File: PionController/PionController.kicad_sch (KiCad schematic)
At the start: 1 part, among them U1 STM32H743VITx

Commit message: power
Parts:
- U1: LCSC (none) -> C1235410; Manufacturer (none) -> stm32f413vgt3
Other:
- added sheet power (untitled.kicad_sch)
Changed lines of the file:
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@@
+			)
+		)
+		(property "LCSC" "C1235410"
+			(at 106.68 100.33 0)
+			(effects
+				(font
+					(size 1.27 1.27)
+				)
+				(hide yes)
+			)
+		)
+		(property "Manufacturer" "stm32f413vgt3"
+			(at 106.68 100.33 0)
+			(effects
+				(font
+					(size 1.27 1.27)
+				)
+				(hide yes)
 			)
 		)
@@
 				)
 			)
+		)
+	)
+	(sheet
+		(at 387.35 137.16)
+		(size 34.29 31.75)
+		(fields_autoplaced yes)
+		(stroke
+			(width 0.1524)
+			(type solid)
+		)
+		(fill
+			(color 0 0 0 0.0000)
+		)
+		(property "Sheetname" "power"
+			(at 387.35 136.4484 0)
+			(effects
+				(font
+					(size 1.27 1.27)
+				)
+				(justify left bottom)
+			)
+		)
+		(property "Sheetfile" "untitled.kicad_sch"
+			(at 387.35 169.4946 0)
+			(effects
+				(font
+					(size 1.27 1.27)
+				)
+				(justify left top)
+			)
+		)
+		(property "Field2" ""
+			(at 387.35 137.16 0)
+			(effects
+				(font
+					(size 1.27 1.27)
+				)
+				(hide yes)
+			)
+		)
+		(instances
+			(project "PionController"
+				(path "/4c75befe-3f28-4e3b-aaa6-2731a1e568ad"
+					(page "2")
+				)
+			)

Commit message: Power_Fix
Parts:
- removed U1: STM32H743VITx, Package_QFP:LQFP-100_14x14mm_P0.5mm, symbol MCU_ST_STM32H7:STM32H743VITx
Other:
- added sheet Main (main.kicad_sch)

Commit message: Schematic_ready
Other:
- added sheet CAN (CAN.kicad_sch)
- added sheet Connectors (connectors.kicad_sch)
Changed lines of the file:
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@@
 	(paper "A4")
+	(sheet
+		(at 198.12 17.78)
+		(size 39.37 30.48)
+		(fields_autoplaced yes)
+		(stroke
+			(width 0.1524)
+			(type solid)
+		)
+		(fill
+			(color 0 0 0 0.0000)
+		)
+		(property "Sheetname" "CAN"
+			(at 198.12 17.0684 0)
+			(effects
+				(font
+					(size 1.27 1.27)
+				)
+				(justify left bottom)
+			)
+		)
+		(property "Sheetfile" "CAN.kicad_sch"
+			(at 198.12 48.8446 0)
+			(effects
+				(font
+					(size 1.27 1.27)
+				)
+				(justify left top)
+			)
+		)
+		(instances
+			(project "PionController"
+				(path "/4c75befe-3f28-4e3b-aaa6-2731a1e568ad"
+					(page "4")
+				)
+			)
+		)
+	)
 	(sheet
 		(at 245.11 59.69)
@@
 				)
 			)
+		)
+	)
+	(sheet
+		(at 199.39 60.96)
+		(size 38.1 49.53)
+		(fields_autoplaced yes)
+		(stroke
+			(width 0.1524)
+			(type solid)
+		)
+		(fill
+			(color 0 0 0 0.0000)
+		)
+		(property "Sheetname" "Connectors"
+			(at 199.39 60.2484 0)
+			(effects
+				(font
+					(size 1.27 1.27)
+				)
+				(justify left bottom)
+			)
+		)
+		(property "Sheetfile" "connectors.kicad_sch"
+			(at 199.39 111.0746 0)
+			(effects
+				(font
+					(size 1.27 1.27)
+				)
+				(justify left top)
+			)
+		)
+		(instances
+			(project "PionController"
+				(path "/4c75befe-3f28-4e3b-aaa6-2731a1e568ad"
+					(page "5")
+				)
+			)

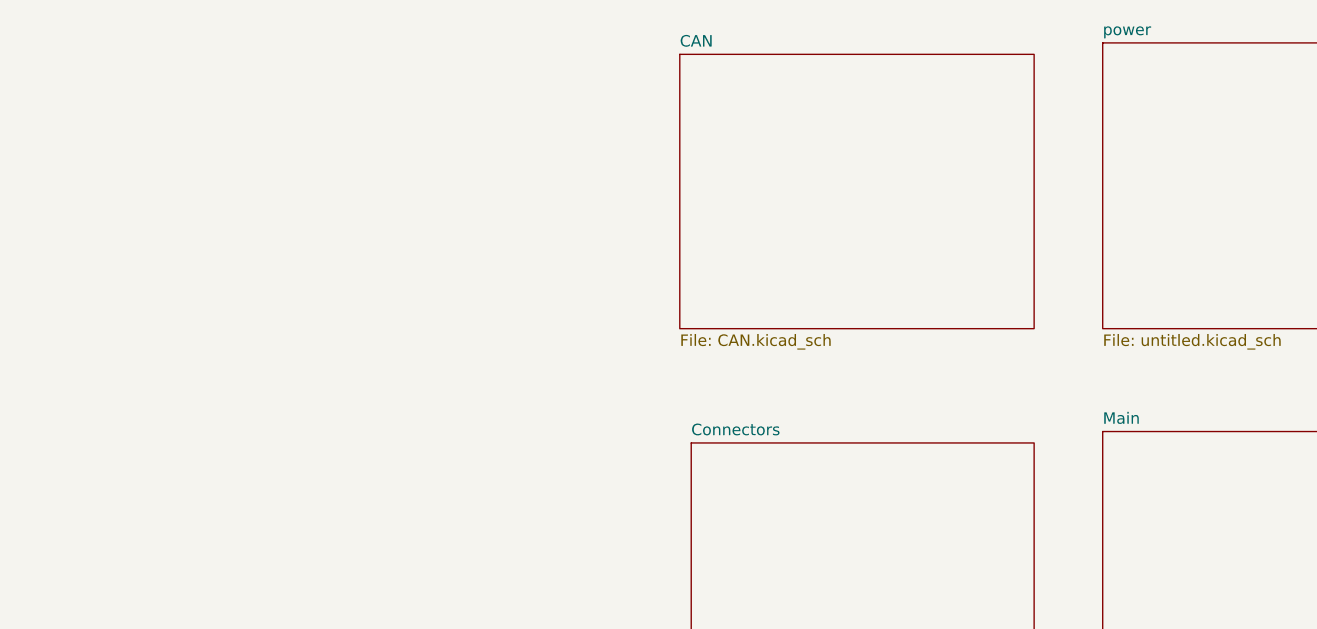
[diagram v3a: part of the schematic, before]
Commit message: adding board outline
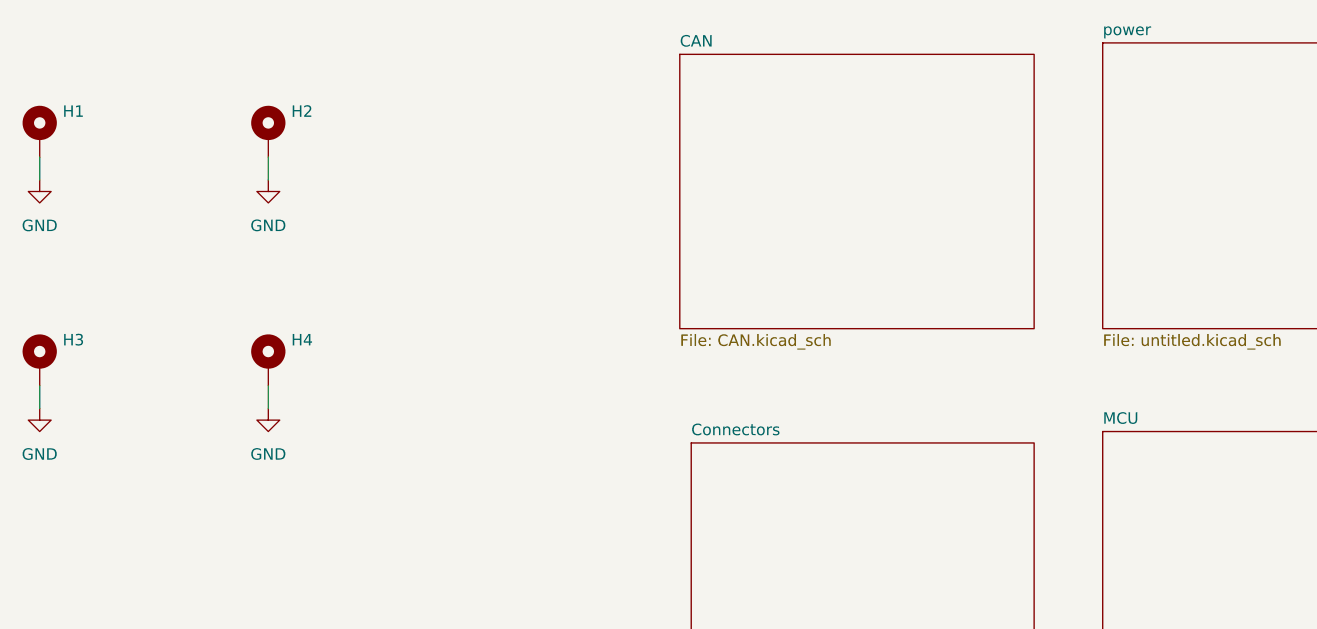
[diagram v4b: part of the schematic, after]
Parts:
- added H1, H2, H3, H4: MountingHole_Pad, MountingHole:MountingHole_3.2mm_M3_Pad_Via, symbol Mechanical:MountingHole_Pad
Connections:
- new net GND: H1.1, H2.1, H3.1, H4.1
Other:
- sheet Main renamed MCU

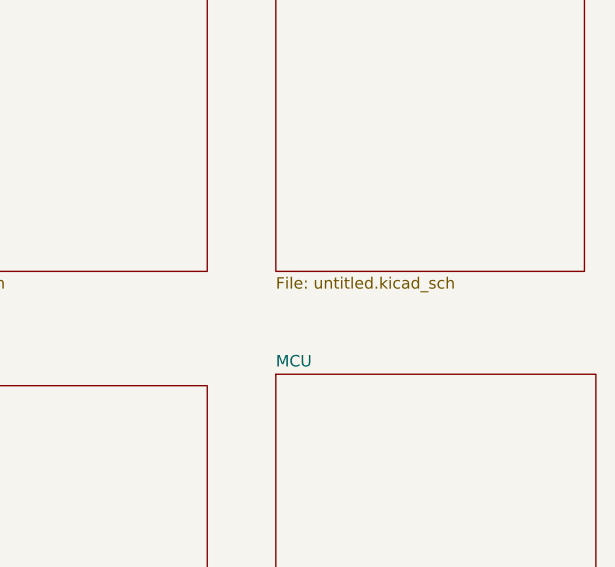
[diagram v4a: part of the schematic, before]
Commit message: Fixing Ivan's remarks and adding the forgotten pull-down resistor
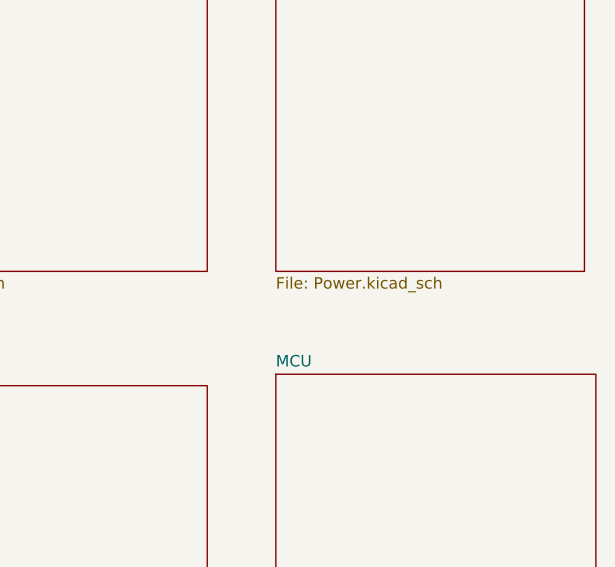
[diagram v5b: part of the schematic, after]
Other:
- sheet power: file untitled.kicad_sch -> Power.kicad_sch
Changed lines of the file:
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@@
 			)
 		)
-		(property "Sheetfile" "untitled.kicad_sch"
+		(property "Sheetfile" "Power.kicad_sch"
 			(at 245.11 48.8446 0)
 			(effects

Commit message: Fixed reference designators in SCH and moved PCB silkscreen positions for better visibility
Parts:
- H1, H2, H3, H4: LCSC (none) -> N/A
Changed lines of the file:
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@@
+			)
+		)
+		(property "Package/Footprint" ""
+			(at 127 26.67 0)
+			(effects
+				(font
+					(size 1.27 1.27)
+				)
+				(hide yes)
+			)
+		)
+		(property "LCSC" "N/A"
+			(at 127 26.67 0)
+			(effects
+				(font
+					(size 1.27 1.27)
+				)
+				(hide yes)
 			)
 		)
@@
 			)
 		)
+		(property "Package/Footprint" ""
+			(at 152.4 52.07 0)
+			(effects
+				(font
+					(size 1.27 1.27)
+				)
+				(hide yes)
+			)
+		)
+		(property "LCSC" "N/A"
+			(at 152.4 52.07 0)
+			(effects
+				(font
+					(size 1.27 1.27)
+				)
+				(hide yes)
+			)
+		)
 		(pin "1"
 		)
@@
 			)
 		)
+		(property "Package/Footprint" ""
+			(at 152.4 26.67 0)
+			(effects
+				(font
+					(size 1.27 1.27)
+				)
+				(hide yes)
+			)
+		)
+		(property "LCSC" "N/A"
+			(at 152.4 26.67 0)
+			(effects
+				(font
+					(size 1.27 1.27)
+				)
+				(hide yes)
+			)
+		)
 		(pin "1"
 		)
@@
 			)
 		)
+		(property "Package/Footprint" ""
+			(at 127 52.07 0)
+			(effects
+				(font
+					(size 1.27 1.27)
+				)
+				(hide yes)
+			)
+		)
+		(property "LCSC" "N/A"
+			(at 127 52.07 0)
+			(effects
+				(font
+					(size 1.27 1.27)
+				)
+				(hide yes)
+			)
+		)
 		(pin "1"
 		)
@@
 			(project "PionController"
 				(path "/4c75befe-3f28-4e3b-aaa6-2731a1e568ad"
-					(page "2")
+					(page "3")
 				)
 			)
@@
 			(project "PionController"
 				(path "/4c75befe-3f28-4e3b-aaa6-2731a1e568ad"
-					(page "3")
-				)
-			)
+					(page "2")
+				)
+			)
